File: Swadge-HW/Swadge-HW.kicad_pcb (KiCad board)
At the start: 2 copper layers, 62 x 101 mm, 90 parts, among them J1 Conn_02x03_Odd_Even, J2 PJ-307C, J3 Conn_01x05_Male, P1 USB_C_Plug_USB2.0, Q1 Q_PMOS_GSD, SW1 YTS-D003-1A, SW2 YTS-D003-1A, SW3 YTS-D003-1A, SW4 YTS-D003-1A, SW5 YTS-D003-1A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

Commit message: Fully routed
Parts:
- C17, C4, C5, R4: moved to B.Cu
- moved C17 69.5 mm to (140.0, 114.4), turned to 180 degrees
- moved D5 68.1 mm to (142.6, 115.2), turned to 60 degrees
- moved D6 60.1 mm to (142.6, 109.9), turned to 120 degrees
- moved C5 59.6 mm to (138.0, 112.9), turned to 0 degrees
- moved R4 57.2 mm to (139.6, 104.3), turned to 90 degrees
- moved D4 54.2 mm to (138.0, 117.8), turned to 0 degrees
- moved D3 53.1 mm to (133.5, 115.2), turned to -60 degrees
- moved C4 51.7 mm to (139.1, 109.2), turned to 0 degrees
- moved D1 50.9 mm to (138.0, 107.3), turned to 180 degrees
- moved D2 44.6 mm to (133.5, 109.9), turned to -120 degrees
- moved R11 8.95 mm to (161.1, 88.6)
- moved R15 8.95 mm to (161.1, 95.1)
- moved R16 8.95 mm to (161.1, 91.9)
- moved R17 8.95 mm to (161.1, 90.2)
- moved R10 8.95 mm to (161.1, 87.0)
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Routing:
- net 3V3: track 214.3 -> 278.8 mm, vias 8 -> 16
- net LED: track 0.00 -> 51.4 mm, vias 0 -> 4
- net GND: track 49.7 -> 66.9 mm, vias 9 -> 31
- net Net-(U4-Top_Left): track 29.6 -> 40.1 mm
- net Net-(U4-Bottom): track 17.2 -> 27.3 mm
- net TOUCH_3: track 39.3 -> 30.7 mm
- net TOUCH_2: track 38.6 -> 30.4 mm
- net Net-(U4-Center): track 42.7 -> 50.7 mm
- net TOUCH_4: track 40.1 -> 32.2 mm
- net TOUCH_1: track 37.9 -> 30.1 mm
- net Net-(U4-Top_Right): track 24.6 -> 32.3 mm
- net Net-(U4-Left): track 34.7 -> 42.3 mm
- net TOUCH_5: track 42.1 -> 34.7 mm
- net TOUCH_6: track 44.0 -> 37.4 mm
- net SDA: track 58.4 -> 64.1 mm, vias 7 -> 5
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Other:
- outline, holes or cut-outs redrawn

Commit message: Routing fun
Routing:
- net BTN_1: track 95.8 -> 81.2 mm
- net GND: track 66.9 -> 70.1 mm, vias 31 -> 147
- net BTN_4: track 64.7 -> 67.7 mm
- net LED: track 51.4 -> 48.9 mm
- net Net-(U8-VO1): track 40.5 -> 41.6 mm
- net BTN_2: track 56.8 -> 55.7 mm
- net 3V3: track 278.8 -> 279.8 mm
- net BTN_5: track 86.5 -> 87.3 mm

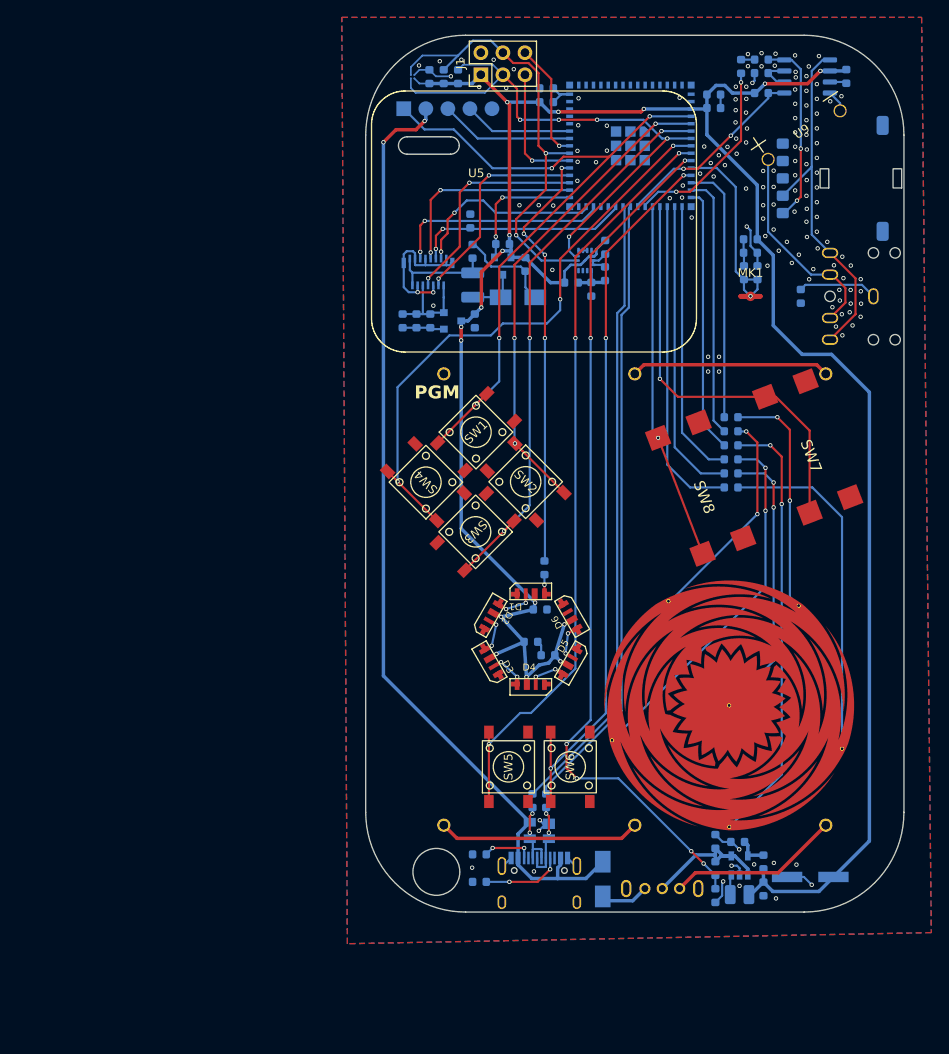
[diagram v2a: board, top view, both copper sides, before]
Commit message: Fillet tracks, fix SAO, vias
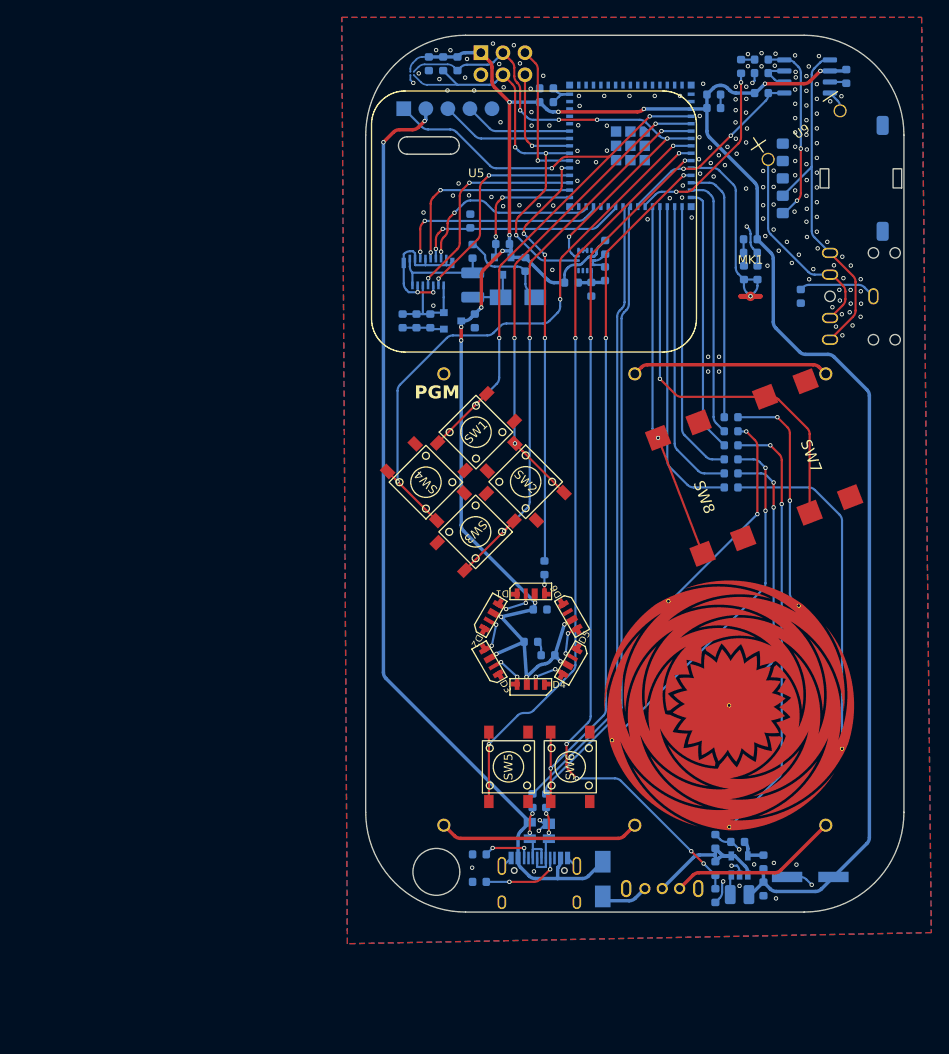
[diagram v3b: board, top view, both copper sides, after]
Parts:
- J1: moved to B.Cu
- moved J1 2.54 mm to (132.3, 45.0), turned to -90 degrees
- moved C21 1.49 mm to (126.3, 46.3), turned to -90 degrees
- moved R6 1.49 mm to (127.9, 46.3), turned to 90 degrees
- moved R18 1.49 mm to (129.6, 46.3), turned to -90 degrees
- moved U10 0.38 mm to (124.3, 47.4), turned to 0 degrees
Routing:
- net SDA: track 64.1 -> 58.6 mm
- net GND: track 70.1 -> 65.7 mm, vias 147 -> 174
- net SCL: track 52.1 -> 47.7 mm, vias 2 -> 3
- net GPIO40: track 14.5 -> 16.7 mm
- net 3V3: track 279.8 -> 281.9 mm
- net GPIO42: track 13.6 -> 12.8 mm

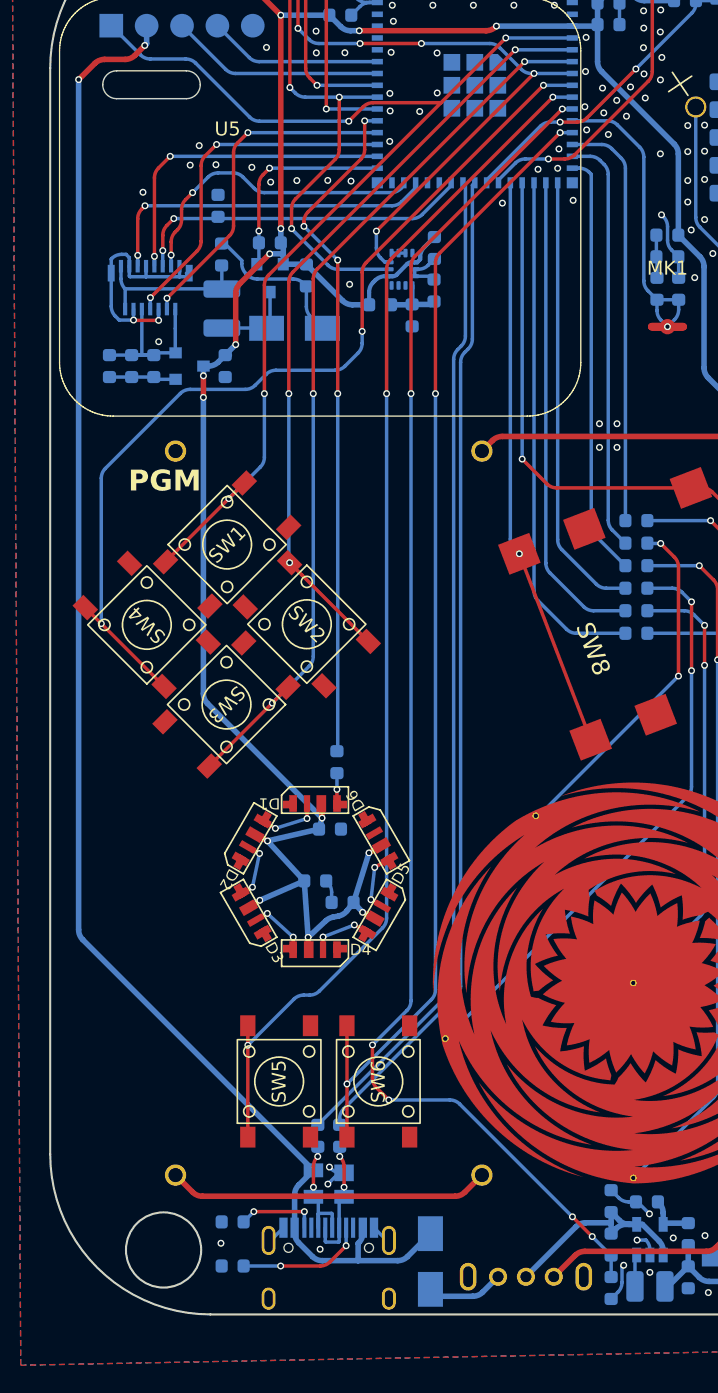
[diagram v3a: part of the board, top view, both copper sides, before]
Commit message: Fixed button placement
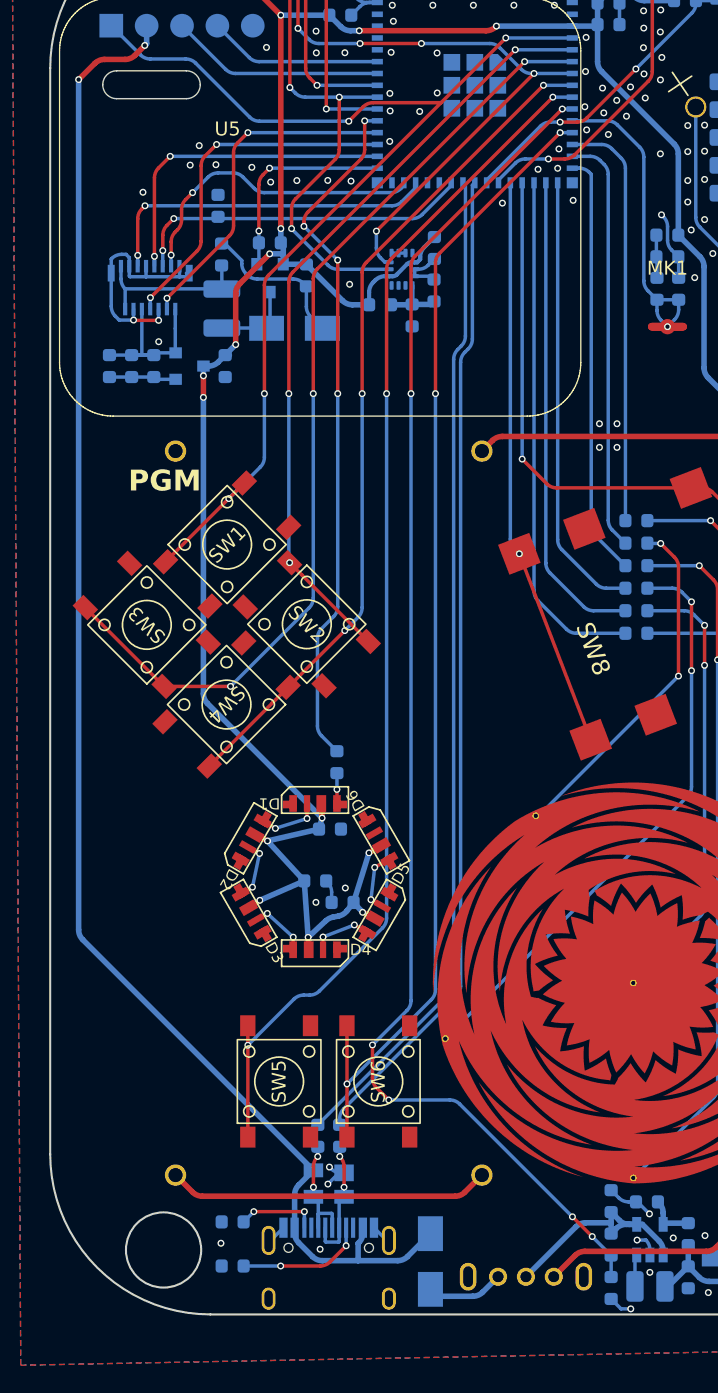
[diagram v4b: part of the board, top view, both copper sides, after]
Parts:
- moved SW3 8.09 mm to (125.9, 94.5), turned to 135 degrees
- moved SW4 8.09 mm to (131.7, 100.2), turned to -135 degrees
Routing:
- net BTN_4: track 67.3 -> 60.8 mm
- net BTN_3: track 64.9 -> 69.7 mm
- net LED: track 48.8 -> 49.9 mm
- net GND: track 65.7 -> 64.6 mm, vias 174 -> 176

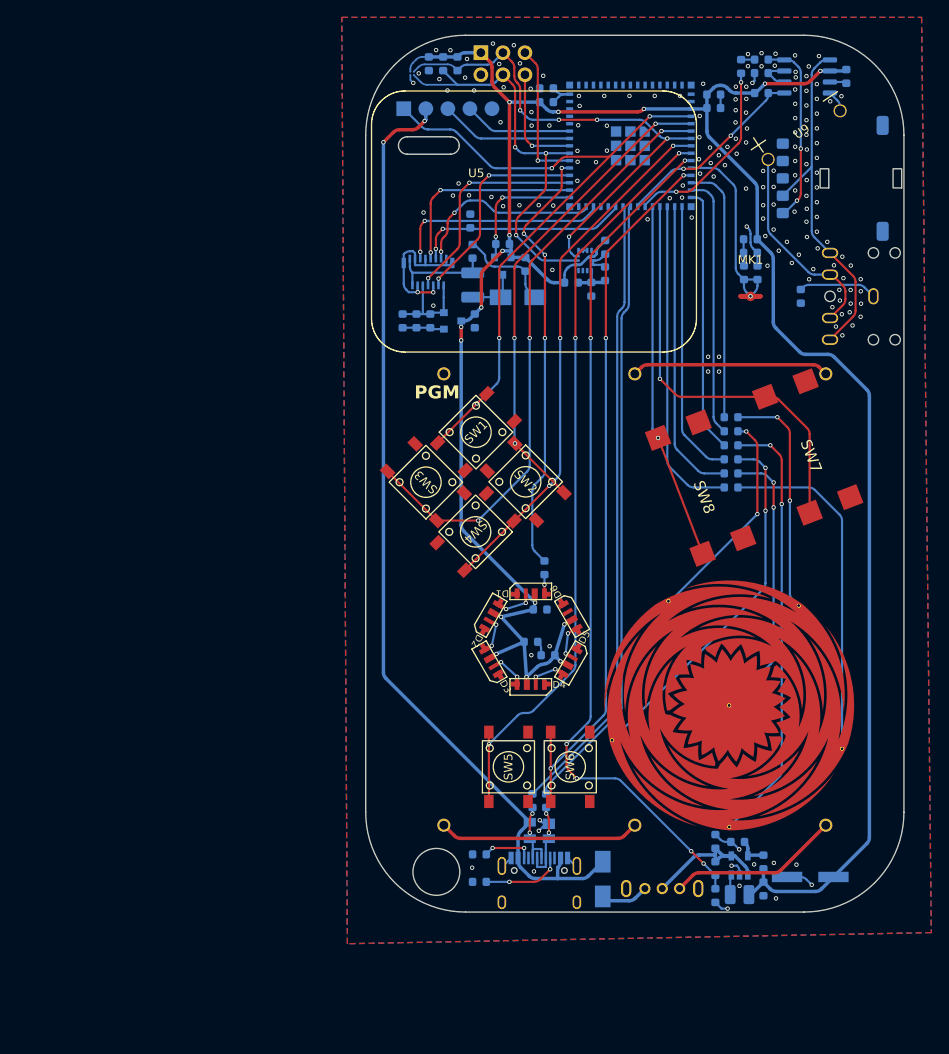
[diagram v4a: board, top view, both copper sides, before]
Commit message: Update touchpad
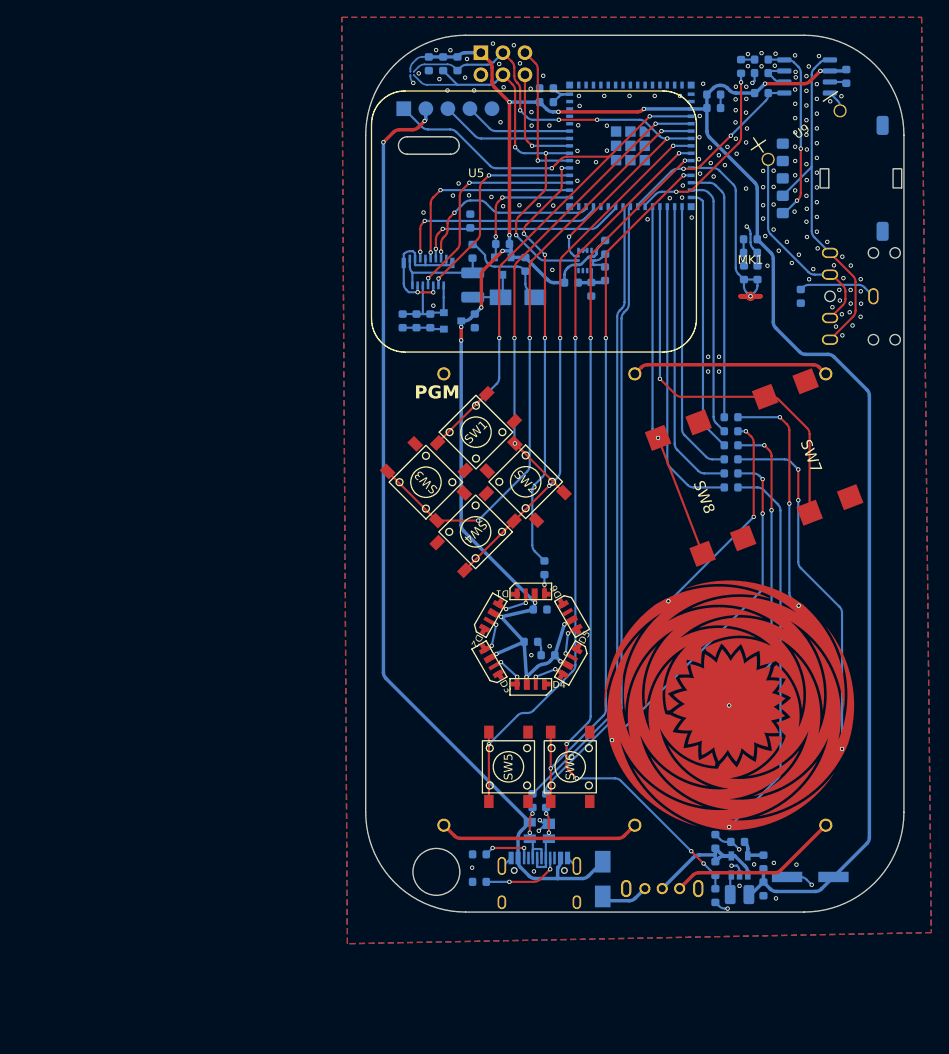
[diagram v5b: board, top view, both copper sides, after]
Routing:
- net Net-(U4-Center): track 50.7 -> 35.3 mm, vias 2 -> 3
- net Net-(U4-Top_Right): track 32.2 -> 40.3 mm, vias 2 -> 3
- net Net-(U4-Top_Left): track 40.0 -> 45.0 mm, vias 0 -> 1
- net Net-(U4-Left): track 42.2 -> 41.6 mm, vias 2 -> 3
- net Net-(U4-Right): track 25.3 -> 25.0 mm, vias 2 -> 3
- net Net-(U4-Bottom): track 27.2 -> 27.3 mm, vias 2 -> 3

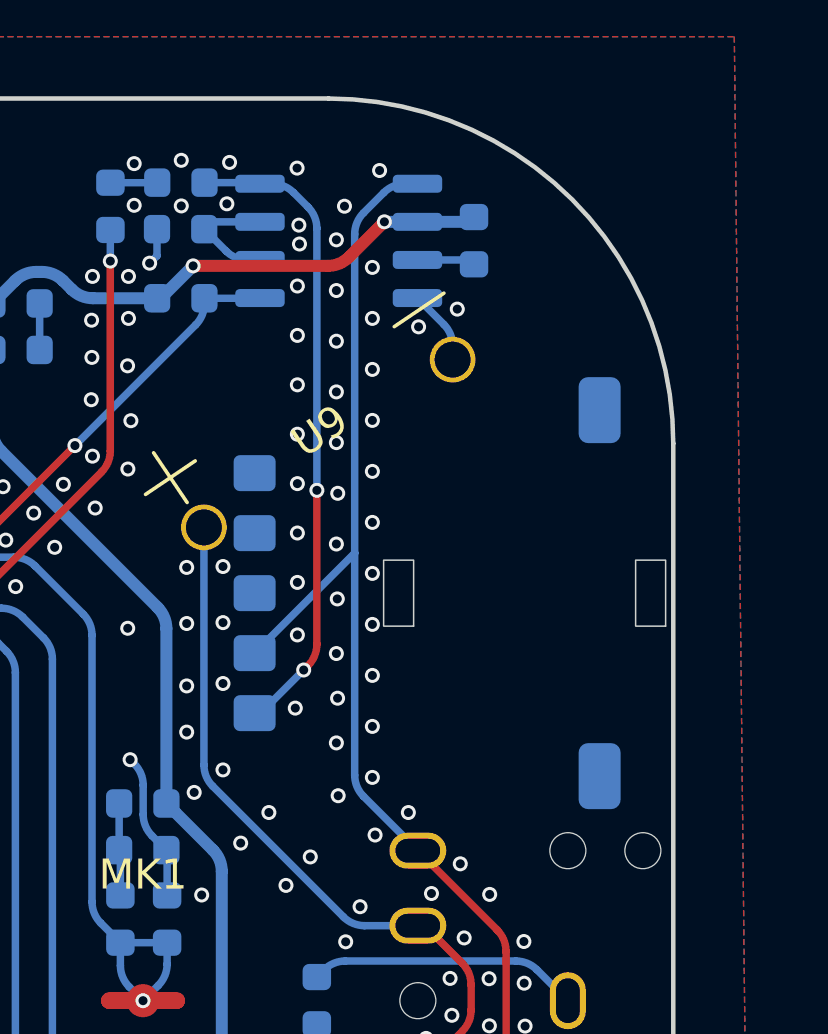
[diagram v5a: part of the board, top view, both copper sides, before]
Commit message: Sync PCB with SCH
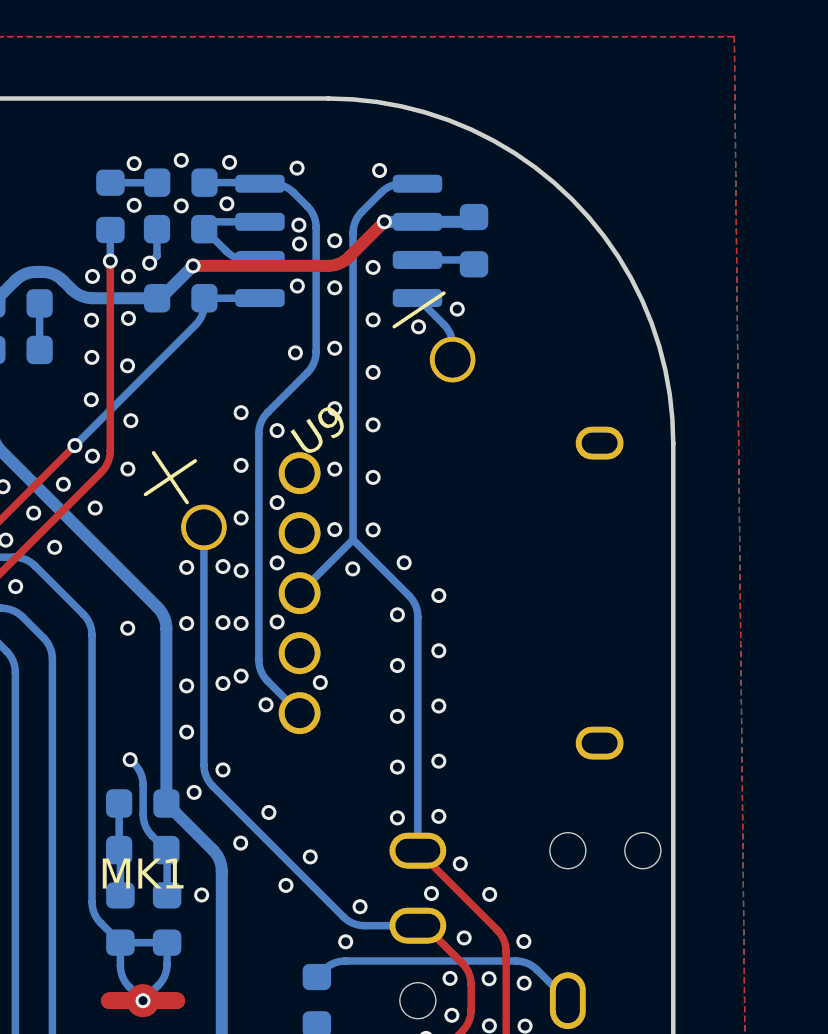
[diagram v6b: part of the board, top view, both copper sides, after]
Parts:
- RV1: footprint Swadge_Parts:RK10J11R001Y -> Swadge_Parts:RK10J11E0034
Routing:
- net Net-(U8-VO1): track 41.4 -> 39.3 mm
- net Net-(U8-IN-): track 21.4 -> 21.8 mm, vias 2 -> 0
- net GND: vias 176 -> 179
